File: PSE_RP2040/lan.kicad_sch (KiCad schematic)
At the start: 32 parts, among them IC1 LAN8742A-CZ, T1 749013011, U4 USBLC6-4SC6, Y3 25MHz

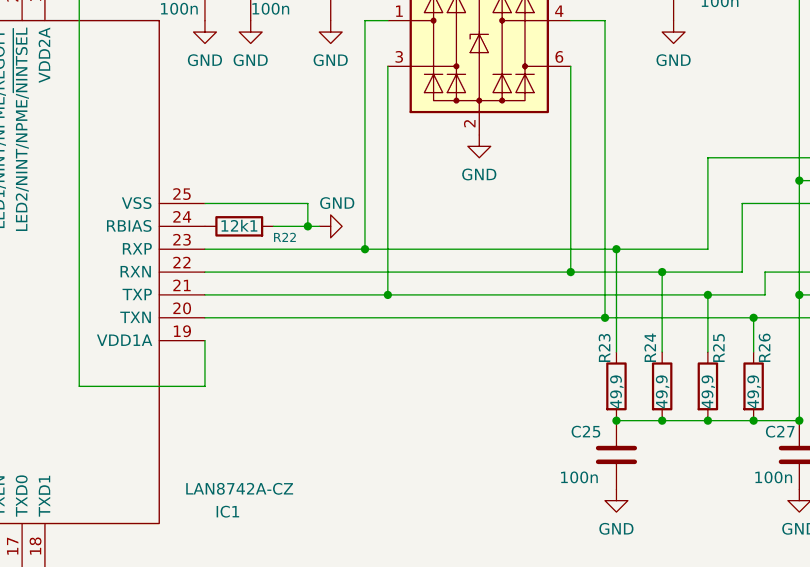
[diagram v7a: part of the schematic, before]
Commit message: modifiche schematico e pcb
Invertito tx e rx  tra trasformatore e modulo lan per sbroglio più comodo.
Fatto posto per allontanare gps dal bordo e collegate varie cose
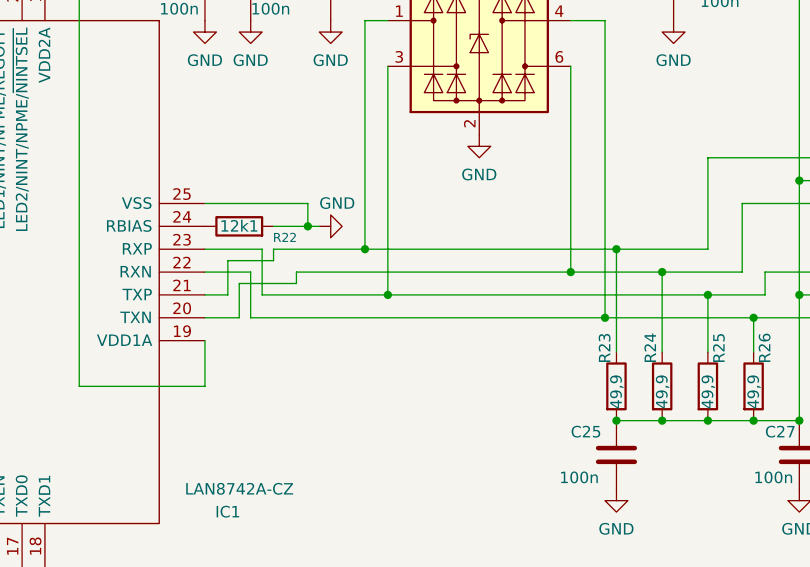
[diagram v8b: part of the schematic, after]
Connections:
- net at R23.1, T1.1 (RD+), U4.1 (I/O1): now also IC1.21 (TXP); no longer IC1.23 (RXP)
- net at R24.1, T1.3 (RD-), U4.6 (I/O4): now also IC1.20 (TXN); no longer IC1.22 (RXN)
- net at R25.1, T1.6 (TD+), U4.3 (I/O2): now also IC1.23 (RXP); no longer IC1.21 (TXP)
- net at R26.1, T1.8 (TD-), U4.4 (I/O3): now also IC1.22 (RXN); no longer IC1.20 (TXN)
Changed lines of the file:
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@@
   (junction (at 99.06 30.48) (diameter 0) (color 0 0 0 0)
   )
+  (junction (at 127 63.5) (diameter 0) (color 0 0 0 0)
+  )
+  (junction (at 182.88 115.57) (diameter 0) (color 0 0 0 0)
+  )
+  (junction (at 177.8 101.6) (diameter 0) (color 0 0 0 0)
+  )
+  (junction (at 172.72 99.06) (diameter 0) (color 0 0 0 0)
+  )
+  (junction (at 27.94 93.98) (diameter 0) (color 0 0 0 0)
+  )
+  (junction (at 187.96 115.57) (diameter 0) (color 0 0 0 0)
+  )
+  (junction (at 167.64 96.52) (diameter 0) (color 0 0 0 0)
+  )
+  (junction (at 133.35 93.98) (diameter 0) (color 0 0 0 0)
+  )
+  (junction (at 142.24 101.6) (diameter 0) (color 0 0 0 0)
+  )
+  (junction (at 58.42 76.2) (diameter 0) (color 0 0 0 0)
+  )
+  (junction (at 62.23 138.43) (diameter 0) (color 0 0 0 0)
+  )
+  (junction (at 177.8 115.57) (diameter 0) (color 0 0 0 0)
+  )
   (junction (at 162.56 99.06) (diameter 0) (color 0 0 0 0)
   )
+  (junction (at 187.96 88.9) (diameter 0) (color 0 0 0 0)
+  )
+  (junction (at 91.44 30.48) (diameter 0) (color 0 0 0 0)
+  )
+  (junction (at 50.8 91.44) (diameter 0) (color 0 0 0 0)
+  )
+  (junction (at 182.88 104.14) (diameter 0) (color 0 0 0 0)
+  )
+  (junction (at 54.61 101.6) (diameter 0) (color 0 0 0 0)
+  )
+  (junction (at 135.89 63.5) (diameter 0) (color 0 0 0 0)
+  )
+  (junction (at 104.14 66.04) (diameter 0) (color 0 0 0 0)
+  )
+  (junction (at 152.4 63.5) (diameter 0) (color 0 0 0 0)
+  )
+  (junction (at 77.47 55.88) (diameter 0) (color 0 0 0 0)
+  )
+  (junction (at 166.37 104.14) (diameter 0) (color 0 0 0 0)
+  )
+  (junction (at 50.8 76.2) (diameter 0) (color 0 0 0 0)
+  )
+  (junction (at 58.42 104.14) (diameter 0) (color 0 0 0 0)
+  )
+  (junction (at 54.61 76.2) (diameter 0) (color 0 0 0 0)
+  )
   (junction (at 139.7 96.52) (diameter 0) (color 0 0 0 0)
-  )
-  (junction (at 127 63.5) (diameter 0) (color 0 0 0 0)
-  )
-  (junction (at 182.88 115.57) (diameter 0) (color 0 0 0 0)
-  )
-  (junction (at 177.8 101.6) (diameter 0) (color 0 0 0 0)
-  )
-  (junction (at 172.72 99.06) (diameter 0) (color 0 0 0 0)
-  )
-  (junction (at 166.37 104.14) (diameter 0) (color 0 0 0 0)
-  )
-  (junction (at 27.94 93.98) (diameter 0) (color 0 0 0 0)
-  )
-  (junction (at 187.96 115.57) (diameter 0) (color 0 0 0 0)
-  )
-  (junction (at 167.64 96.52) (diameter 0) (color 0 0 0 0)
-  )
-  (junction (at 133.35 93.98) (diameter 0) (color 0 0 0 0)
-  )
-  (junction (at 58.42 76.2) (diameter 0) (color 0 0 0 0)
-  )
-  (junction (at 142.24 101.6) (diameter 0) (color 0 0 0 0)
-  )
-  (junction (at 62.23 138.43) (diameter 0) (color 0 0 0 0)
-  )
-  (junction (at 177.8 115.57) (diameter 0) (color 0 0 0 0)
-  )
-  (junction (at 187.96 88.9) (diameter 0) (color 0 0 0 0)
-  )
-  (junction (at 91.44 30.48) (diameter 0) (color 0 0 0 0)
-  )
-  (junction (at 50.8 91.44) (diameter 0) (color 0 0 0 0)
-  )
-  (junction (at 182.88 104.14) (diameter 0) (color 0 0 0 0)
-  )
-  (junction (at 54.61 101.6) (diameter 0) (color 0 0 0 0)
-  )
-  (junction (at 135.89 63.5) (diameter 0) (color 0 0 0 0)
-  )
-  (junction (at 104.14 66.04) (diameter 0) (color 0 0 0 0)
-  )
-  (junction (at 152.4 63.5) (diameter 0) (color 0 0 0 0)
-  )
-  (junction (at 77.47 55.88) (diameter 0) (color 0 0 0 0)
-  )
-  (junction (at 50.8 76.2) (diameter 0) (color 0 0 0 0)
-  )
-  (junction (at 58.42 104.14) (diameter 0) (color 0 0 0 0)
-  )
-  (junction (at 54.61 76.2) (diameter 0) (color 0 0 0 0)
   )
   (junction (at 167.64 115.57) (diameter 0) (color 0 0 0 0)
@@
     (stroke (width 0) (type default) (color 0 0 0 0))
   )
+  (wire (pts (xy 121.92 96.52) (xy 128.27 96.52))
+    (stroke (width 0) (type default) (color 0 0 0 0))
+  )
   (wire (pts (xy 62.23 83.82) (xy 62.23 138.43))
     (stroke (width 0) (type default) (color 0 0 0 0))
@@
     (stroke (width 0) (type default) (color 0 0 0 0))
   )
+  (wire (pts (xy 128.27 101.6) (xy 142.24 101.6))
+    (stroke (width 0) (type default) (color 0 0 0 0))
+  )
   (wire (pts (xy 152.4 63.5) (xy 173.99 63.5))
     (stroke (width 0) (type default) (color 0 0 0 0))
@@
     (stroke (width 0) (type default) (color 0 0 0 0))
   )
+  (wire (pts (xy 124.46 101.6) (xy 124.46 97.79))
+    (stroke (width 0) (type default) (color 0 0 0 0))
+  )
   (wire (pts (xy 95.25 19.05) (xy 95.25 25.4))
     (stroke (width 0) (type default) (color 0 0 0 0))
@@
     (stroke (width 0) (type default) (color 0 0 0 0))
   )
+  (wire (pts (xy 125.73 104.14) (xy 125.73 100.33))
+    (stroke (width 0) (type default) (color 0 0 0 0))
+  )
+  (wire (pts (xy 121.92 104.14) (xy 125.73 104.14))
+    (stroke (width 0) (type default) (color 0 0 0 0))
+  )
+  (wire (pts (xy 127 99.06) (xy 127 104.14))
+    (stroke (width 0) (type default) (color 0 0 0 0))
+  )
   (wire (pts (xy 63.5 96.52) (xy 27.94 96.52))
     (stroke (width 0) (type default) (color 0 0 0 0))
@@
     (stroke (width 0) (type default) (color 0 0 0 0))
   )
+  (wire (pts (xy 132.08 100.33) (xy 132.08 99.06))
+    (stroke (width 0) (type default) (color 0 0 0 0))
+  )
+  (wire (pts (xy 128.27 96.52) (xy 128.27 101.6))
+    (stroke (width 0) (type default) (color 0 0 0 0))
+  )
   (wire (pts (xy 101.6 55.88) (xy 105.41 55.88))
     (stroke (width 0) (type default) (color 0 0 0 0))
@@
     (stroke (width 0) (type default) (color 0 0 0 0))
   )
+  (wire (pts (xy 121.92 99.06) (xy 127 99.06))
+    (stroke (width 0) (type default) (color 0 0 0 0))
+  )
   (wire (pts (xy 162.56 71.12) (xy 166.37 71.12))
     (stroke (width 0) (type default) (color 0 0 0 0))
@@
     (stroke (width 0) (type default) (color 0 0 0 0))
   )
-  (wire (pts (xy 121.92 96.52) (xy 139.7 96.52))
-    (stroke (width 0) (type default) (color 0 0 0 0))
-  )
   (wire (pts (xy 104.14 66.04) (xy 107.95 66.04))
     (stroke (width 0) (type default) (color 0 0 0 0))
@@
     (stroke (width 0) (type default) (color 0 0 0 0))
   )
-  (wire (pts (xy 121.92 104.14) (xy 166.37 104.14))
-    (stroke (width 0) (type default) (color 0 0 0 0))
-  )
   (wire (pts (xy 35.56 91.44) (xy 38.1 91.44))
     (stroke (width 0) (type default) (color 0 0 0 0))
@@
     (stroke (width 0) (type default) (color 0 0 0 0))
   )
+  (wire (pts (xy 129.54 96.52) (xy 139.7 96.52))
+    (stroke (width 0) (type default) (color 0 0 0 0))
+  )
   (wire (pts (xy 187.96 101.6) (xy 187.96 115.57))
     (stroke (width 0) (type default) (color 0 0 0 0))
@@
     (stroke (width 0) (type default) (color 0 0 0 0))
   )
-  (wire (pts (xy 121.92 101.6) (xy 142.24 101.6))
-    (stroke (width 0) (type default) (color 0 0 0 0))
-  )
   (wire (pts (xy 58.42 76.2) (xy 62.23 76.2))
     (stroke (width 0) (type default) (color 0 0 0 0))
@@
     (stroke (width 0) (type default) (color 0 0 0 0))
   )
+  (wire (pts (xy 121.92 101.6) (xy 124.46 101.6))
+    (stroke (width 0) (type default) (color 0 0 0 0))
+  )
   (wire (pts (xy 187.96 101.6) (xy 190.5 101.6))
     (stroke (width 0) (type default) (color 0 0 0 0))
@@
     (stroke (width 0) (type default) (color 0 0 0 0))
   )
+  (wire (pts (xy 127 104.14) (xy 166.37 104.14))
+    (stroke (width 0) (type default) (color 0 0 0 0))
+  )
+  (wire (pts (xy 132.08 99.06) (xy 162.56 99.06))
+    (stroke (width 0) (type default) (color 0 0 0 0))
+  )
   (wire (pts (xy 38.1 99.06) (xy 36.83 99.06))
     (stroke (width 0) (type default) (color 0 0 0 0))
   )
-  (wire (pts (xy 121.92 99.06) (xy 162.56 99.06))
-    (stroke (width 0) (type default) (color 0 0 0 0))
-  )
   (wire (pts (xy 46.99 83.82) (xy 46.99 93.98))
     (stroke (width 0) (type default) (color 0 0 0 0))
@@
     (stroke (width 0) (type default) (color 0 0 0 0))
   )
+  (wire (pts (xy 124.46 97.79) (xy 129.54 97.79))
+    (stroke (width 0) (type default) (color 0 0 0 0))
+  )
   (wire (pts (xy 57.15 76.2) (xy 57.15 74.93))
     (stroke (width 0) (type default) (color 0 0 0 0))
   )
+  (wire (pts (xy 125.73 100.33) (xy 132.08 100.33))
+    (stroke (width 0) (type default) (color 0 0 0 0))
+  )
   (wire (pts (xy 121.92 111.76) (xy 107.95 111.76))
     (stroke (width 0) (type default) (color 0 0 0 0))
   )
+  (wire (pts (xy 129.54 97.79) (xy 129.54 96.52))
+    (stroke (width 0) (type default) (color 0 0 0 0))
+  )
